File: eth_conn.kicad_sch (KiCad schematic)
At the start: 30 parts, among them J1 RJ45

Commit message: changed to 4 layer, finished usb conn, added jtag conn, some other things
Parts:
- TP82, TP83, TP84, TP85, TP86, TP87, TP88, TP89: footprint (none) -> TestPoint:TestPoint_THTPad_D1.0mm_Drill0.5mm
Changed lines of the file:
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@@
 			)
 		)
-		(property "Footprint" ""
+		(property "Footprint" "TestPoint:TestPoint_THTPad_D1.0mm_Drill0.5mm"
 			(at 298.45 146.05 0)
 			(hide yes)
@@
 			)
 		)
-		(property "Footprint" ""
+		(property "Footprint" "TestPoint:TestPoint_THTPad_D1.0mm_Drill0.5mm"
 			(at 298.45 153.67 0)
 			(hide yes)
@@
 			)
 		)
-		(property "Footprint" ""
+		(property "Footprint" "TestPoint:TestPoint_THTPad_D1.0mm_Drill0.5mm"
 			(at 298.45 140.97 0)
 			(hide yes)
@@
 			)
 		)
-		(property "Footprint" ""
+		(property "Footprint" "TestPoint:TestPoint_THTPad_D1.0mm_Drill0.5mm"
 			(at 298.45 135.89 0)
 			(hide yes)
@@
 			)
 		)
-		(property "Footprint" ""
+		(property "Footprint" "TestPoint:TestPoint_THTPad_D1.0mm_Drill0.5mm"
 			(at 298.45 138.43 0)
 			(hide yes)
@@
 			)
 		)
-		(property "Footprint" ""
+		(property "Footprint" "TestPoint:TestPoint_THTPad_D1.0mm_Drill0.5mm"
 			(at 298.45 143.51 0)
 			(hide yes)
@@
 			)
 		)
-		(property "Footprint" ""
+		(property "Footprint" "TestPoint:TestPoint_THTPad_D1.0mm_Drill0.5mm"
 			(at 298.45 148.59 0)
 			(hide yes)
@@
 			)
 		)
-		(property "Footprint" ""
+		(property "Footprint" "TestPoint:TestPoint_THTPad_D1.0mm_Drill0.5mm"
 			(at 298.45 151.13 0)
 			(hide yes)

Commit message: many stuffs
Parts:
- removed J1: RJ45, Connector_RJ:RJ45_Amphenol_54602-x08_Horizontal, symbol Connector:RJ45
- removed TR1: PT61017PEL, Transformer_SMD:Transformer_Ethernet_Bourns_PT61017PEL, symbol Transformer:PT61017PEL
- added RJ1: HC-WK88-H16-DB, C7501824:RJ45-TH_HC-WK88-H16-DB, symbol C7501824:HC-WK88-H16-DB
- added T1: H1102NLT, C18584:XFMR-SMD_H1102NLT, symbol C18584:H1102NLT
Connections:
- net CTREF1: now also T1.10
- net CTREF2: now also T1.15
- net ETH_SHIELD: now also RJ1.10, RJ1.9
- net MDI.RX+: now also T1.3
- net MDI.RX-: now also T1.1
- net MDI.TX+: now also T1.8
- net MDI.TX-: now also T1.6
- net MX1+: now also RJ1.1, T1.9
- net MX1-: now also RJ1.2, T1.11
- net MX2+: now also RJ1.3, T1.14
- net MX2-: now also RJ1.6, T1.16
- net MX3+: now also RJ1.4
- net MX3-: now also RJ1.5
- net MX4+: now also RJ1.7
- net MX4-: now also RJ1.8
- net at C35.1: now also T1.2
- net at C34.1: now also T1.7
- no-connect marks 0 -> 4
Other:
- moved on the sheet: C33, C36, C37, D39, R32, R33, R34, R35, R36, R37, R38, R39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

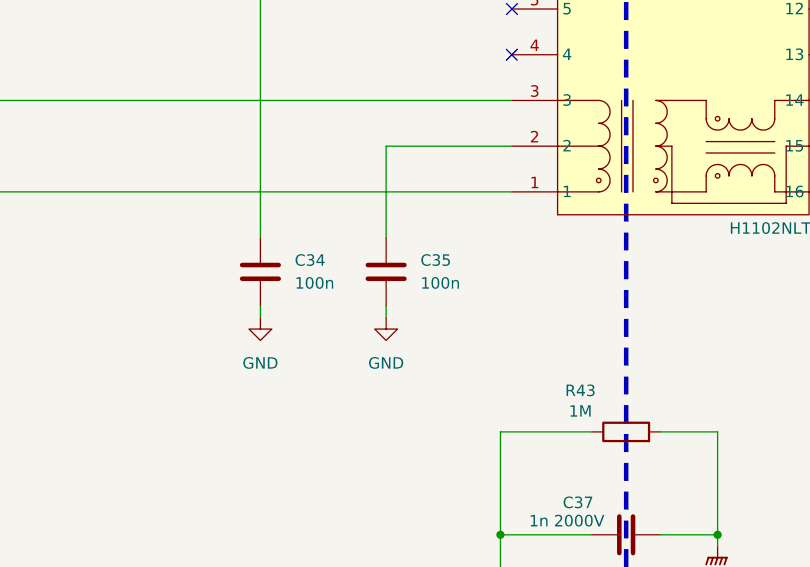
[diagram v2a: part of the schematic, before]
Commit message: did a bunch of bom matching to lcsc
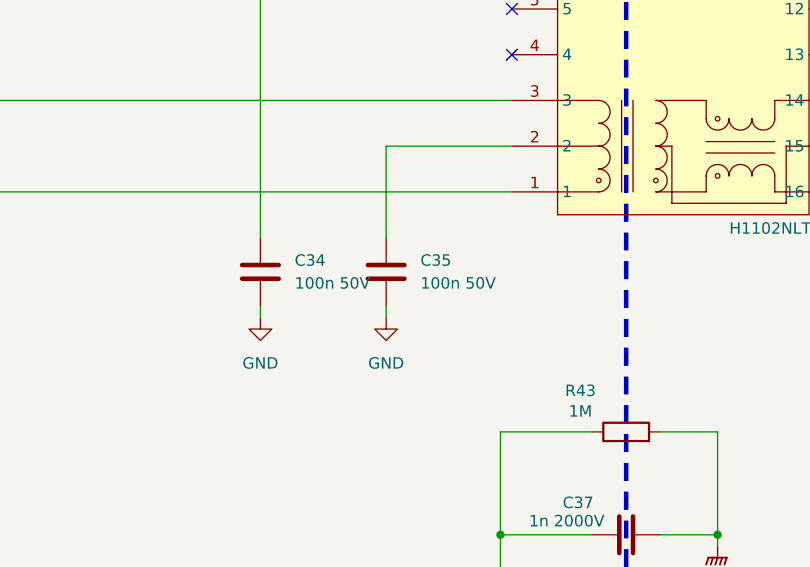
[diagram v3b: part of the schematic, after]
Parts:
- C33, C36, C37: footprint (none) -> Capacitor_SMD:C_1206_3216Metric; LCSC (none) -> C9196; LCSC Basic/Pref (none) -> x; LCSC Part (none) -> C9196
- C34, C35: value 100n -> 100n 50V; LCSC (none) -> C307331; LCSC Basic/Pref (none) -> x; LCSC Part (none) -> C307331
- D39: LCSC Part (none) -> C157526
- R32, R43: footprint (none) -> Resistor_SMD:R_1206_3216Metric; LCSC (none) -> C17927; LCSC Basic/Pref (none) -> x; LCSC Part (none) -> C17927
- R33, R34, R35, R36, R37, R38: LCSC (none) -> C17168; LCSC Basic/Pref (none) -> x; LCSC Part (none) -> C17168
- R39, R40, R41, R42: LCSC (none) -> C25133; LCSC Basic/Pref (none) -> x; LCSC Part (none) -> C25133
- TP82, TP83, TP84, TP85, TP86, TP87, TP88, TP89: now left out of the parts list
- U3, U4: LCSC (none) -> C17566697; LCSC Part (none) -> C17566697

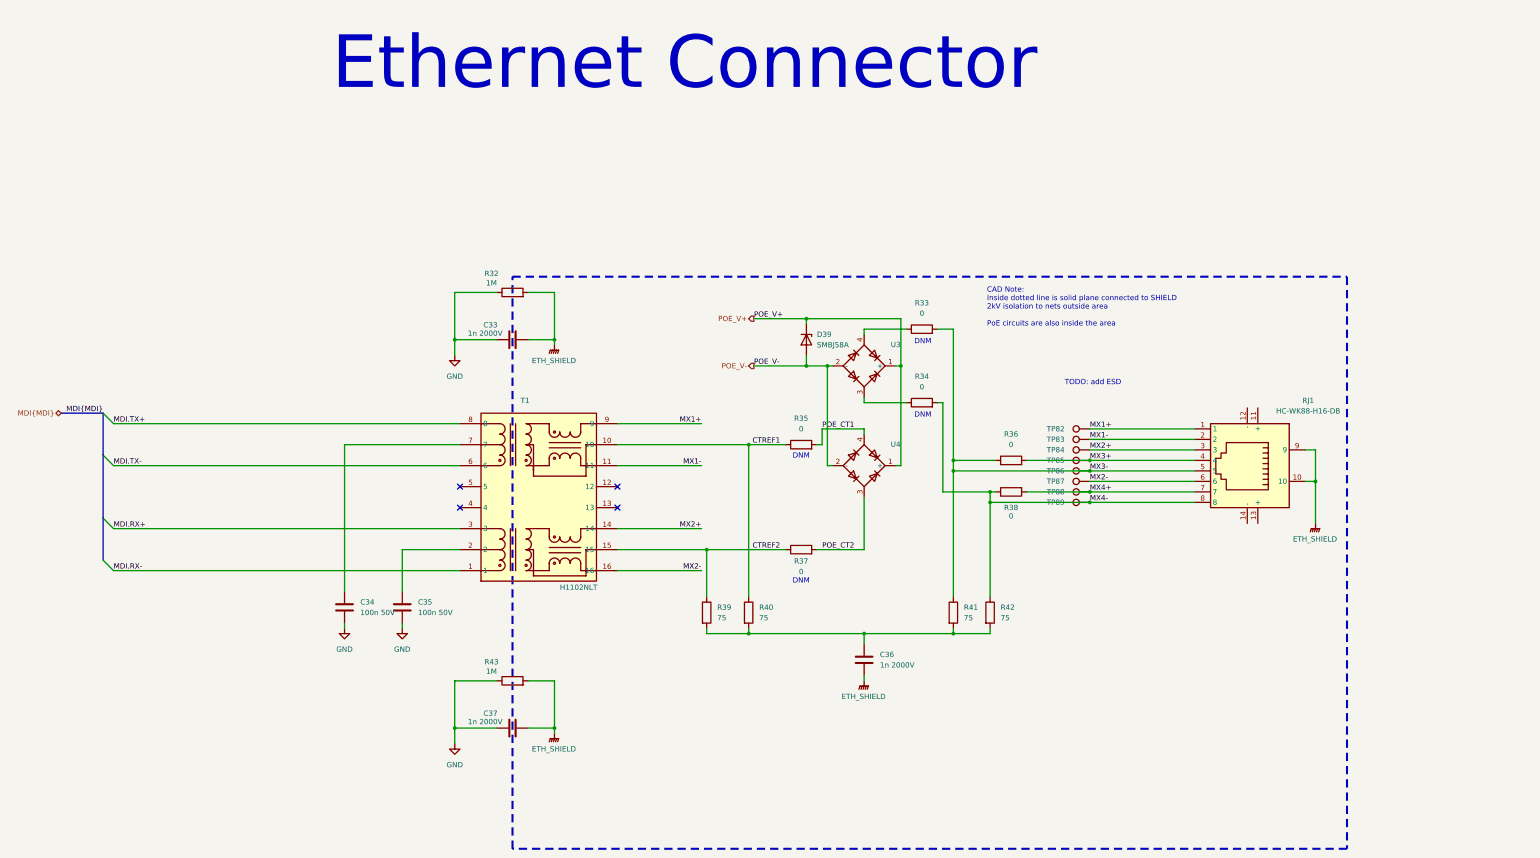
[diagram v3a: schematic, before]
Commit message: did some ethernet, found preferred power switch diode
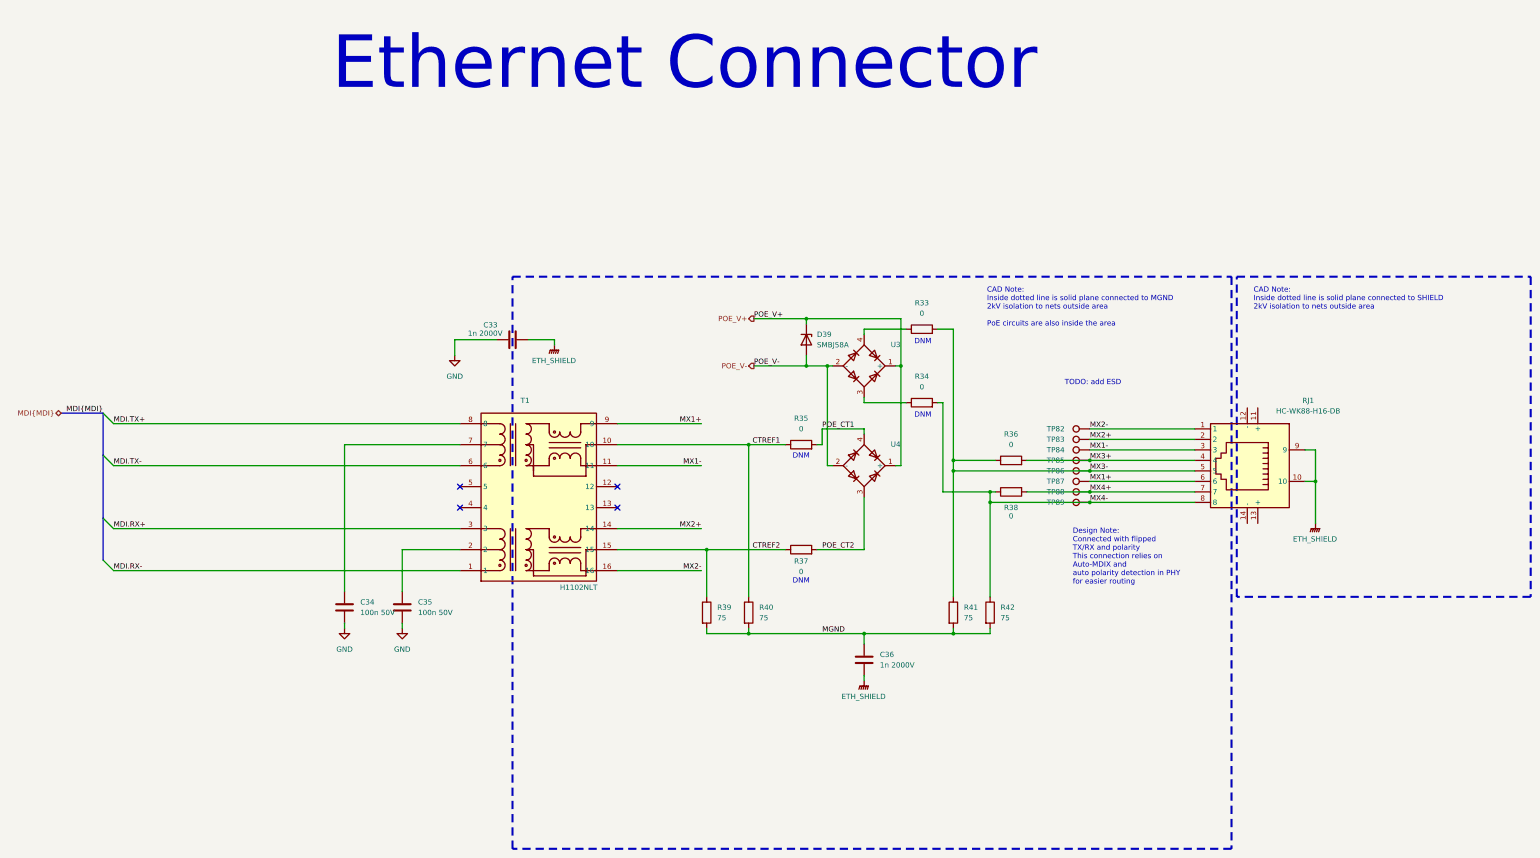
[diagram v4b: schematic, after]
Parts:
- removed C37: 1n 2000V, Capacitor_SMD:C_1206_3216Metric, symbol Device:C
- removed R32, R43: 1M, Resistor_SMD:R_1206_3216Metric, symbol Device:R
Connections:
- net MX1+: now also RJ1.6, TP87.1; no longer RJ1.1, TP82.1
- net MX1-: now also RJ1.3, TP84.1; no longer RJ1.2, TP83.1
- net MX2+: now also RJ1.2, TP83.1; no longer RJ1.3, TP84.1
- net MX2-: now also RJ1.1, TP82.1; no longer RJ1.6, TP87.1
- net MGND: now reaches C36.1, R39.2, R40.2, R41.2, R42.2
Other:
- note added: "CAD Note: Inside dotted line is solid plane connected to MGND 2kV isolation to nets outside area PoE circuits are also inside the area"
- note added: "CAD Note: Inside dotted line is solid plane connected to SHIELD 2kV isolation to nets outside area"
- note removed: "CAD Note: Inside dotted line is solid plane connected to SHIELD 2kV isolation to nets outside area PoE circuits are also inside the area"
